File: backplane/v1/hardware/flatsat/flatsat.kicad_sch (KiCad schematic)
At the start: 0 parts

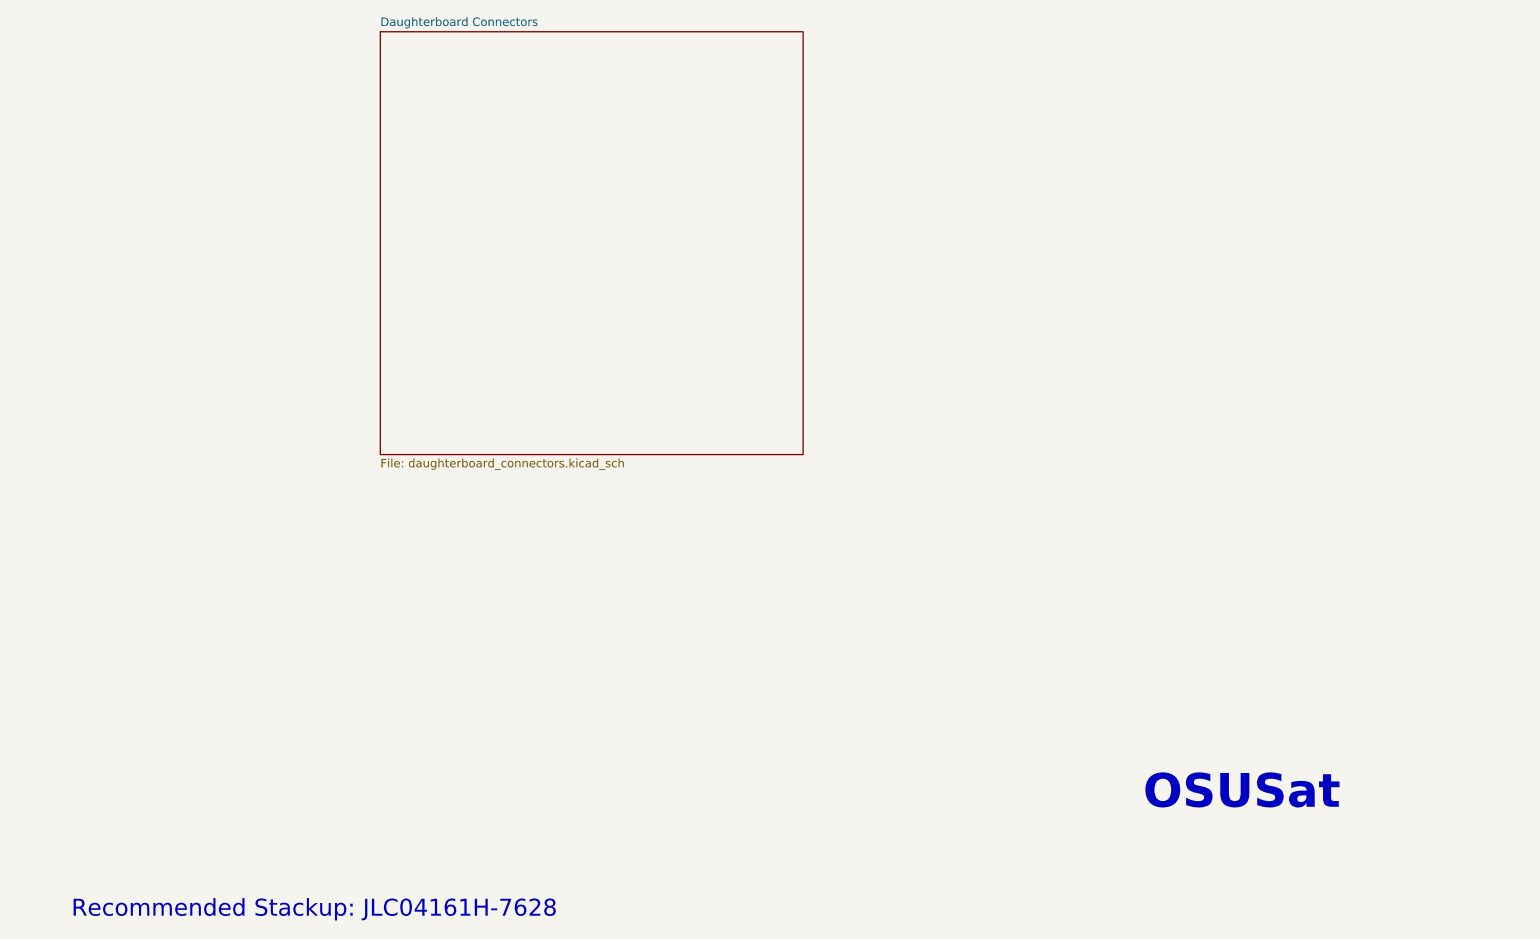
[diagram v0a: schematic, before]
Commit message: fix connector orientation on flatsat
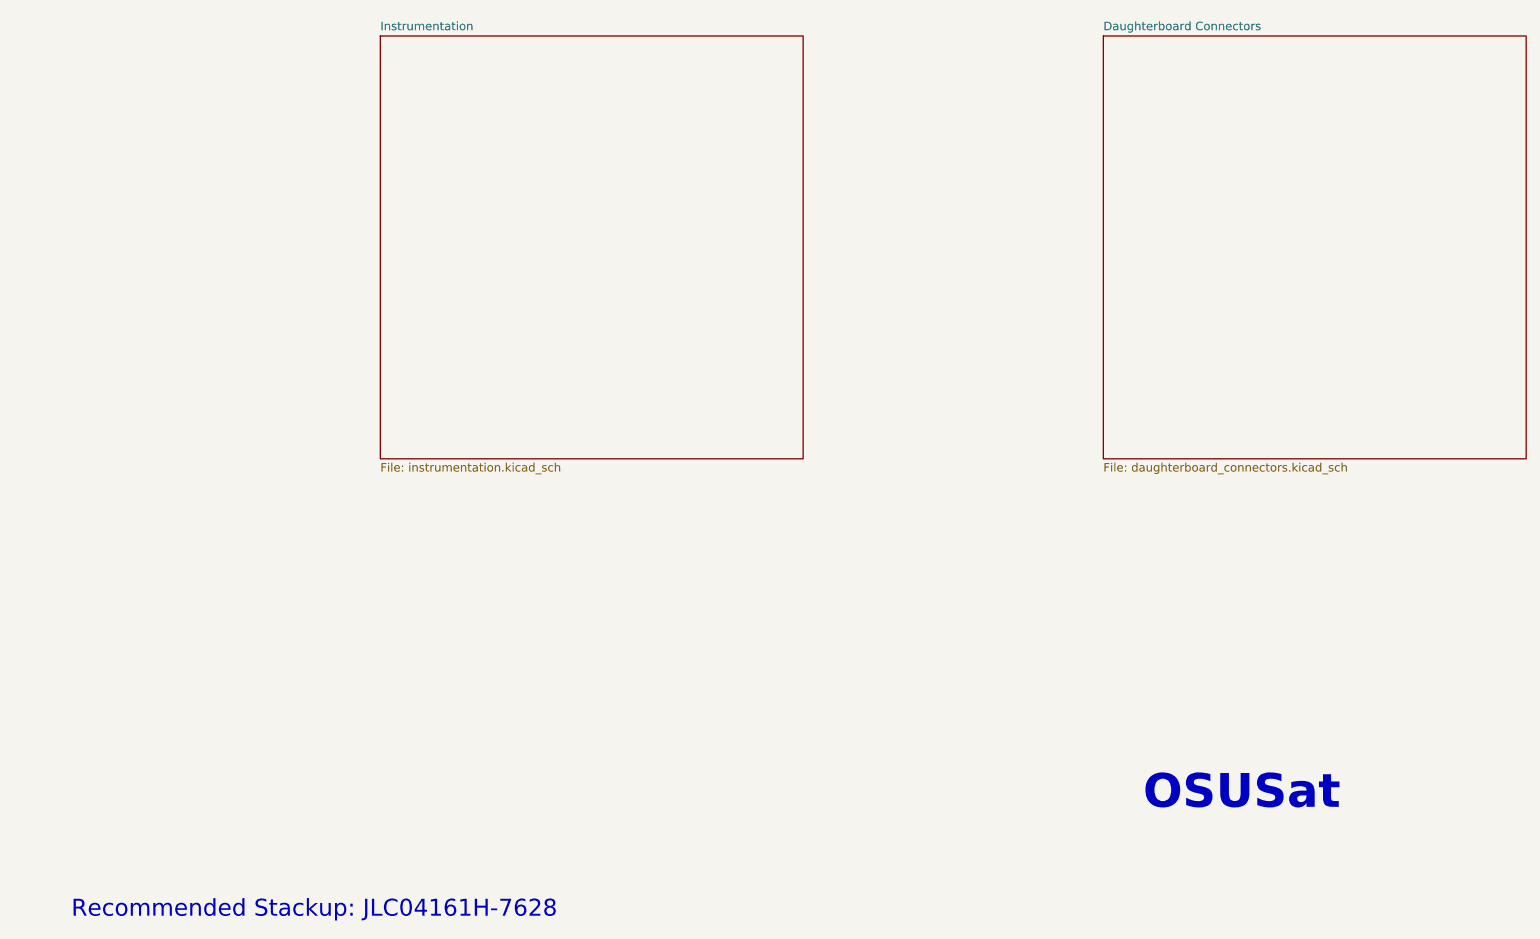
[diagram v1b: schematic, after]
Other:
- added sheet Instrumentation (instrumentation.kicad_sch)
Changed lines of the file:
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@@
 	)
 	(sheet
-		(at 63.5 63.5)
+		(at 63.5 64.135)
+		(size 63.5 63.5)
+		(exclude_from_sim no)
+		(in_bom yes)
+		(on_board yes)
+		(dnp no)
+		(fields_autoplaced yes)
+		(stroke
+			(width 0.1524)
+			(type solid)
+		)
+		(fill
+			(color 255 255 194 1)
+		)
+		(property "Sheetname" "Instrumentation"
+			(at 63.5 63.4234 0)
+			(show_name no)
+			(do_not_autoplace no)
+			(effects
+				(font
+					(size 1.27 1.27)
+				)
+				(justify left bottom)
+			)
+		)
+		(property "Sheetfile" "instrumentation.kicad_sch"
+			(at 63.5 128.2196 0)
+			(show_name no)
+			(do_not_autoplace no)
+			(effects
+				(font
+					(size 1.27 1.27)
+				)
+				(justify left top)
+			)
+		)
+		(instances
+			(project "flatsat"
+				(path "/25068314-cc61-4bab-bc96-a87178fccfab"
+					(page "3")
+				)
+			)
+		)
+	)
+	(sheet
+		(at 172.085 64.135)
 		(size 63.5 63.5)
 		(exclude_from_sim no)
@@
 		)
 		(property "Sheetname" "Daughterboard Connectors"
-			(at 63.5 62.7884 0)
+			(at 172.085 63.4234 0)
 			(show_name no)
 			(do_not_autoplace no)
@@
 		)
 		(property "Sheetfile" "daughterboard_connectors.kicad_sch"
-			(at 63.5 127.5846 0)
+			(at 172.085 128.2196 0)
 			(show_name no)
 			(do_not_autoplace no)
